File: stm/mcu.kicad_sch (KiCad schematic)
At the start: 46 parts, among them J1 Conn_02x07_Odd_Even, J2 SD_Card_Receptacle, SW2 SW_Push, U1 REF4132B25DBVR, U2 STM32H730ZBTx, Y3 Crystal_GND24, Y4 Crystal

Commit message: labels
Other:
- note added: "Resonator with integrated capacitors Datasheet, 6.3.10, figure 24"

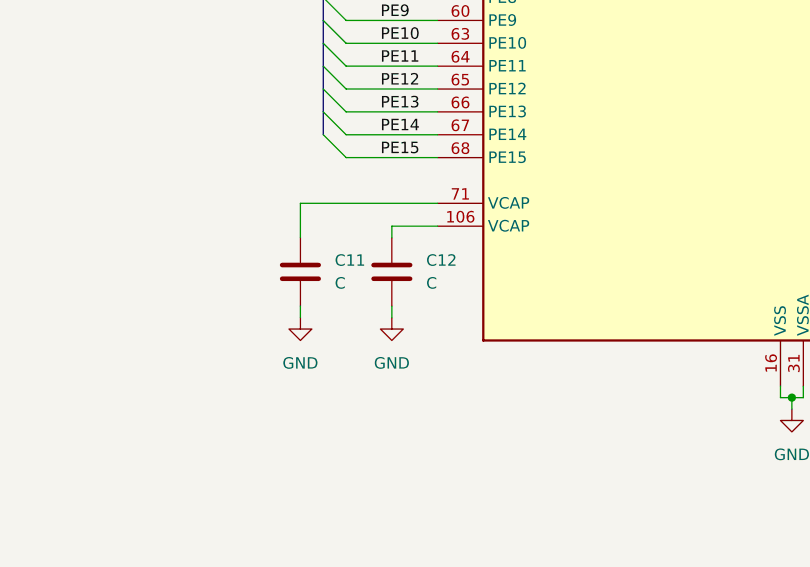
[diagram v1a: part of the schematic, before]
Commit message: vcap on mcu
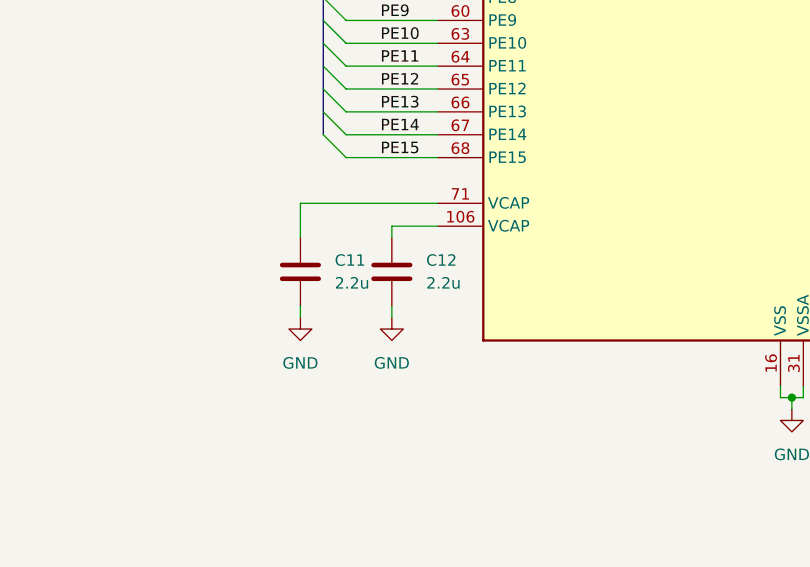
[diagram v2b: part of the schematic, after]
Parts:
- C11, C12: value C -> 2.2u

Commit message: added caps
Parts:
- C1, C10, C15, C16, C17, C18, C19, C21, C22, C23, C24, C25, C26, C3, C7: value C -> 100n
- C13, C14: value C -> 15p
- C2, C20, C4: value C -> 1u
- C27: value C -> 4u7
- C8, C9: value C -> 6p
- R2: value R -> 200k
- Y3: value Crystal_GND24 -> 25MHz
- Y4: value Crystal -> ABS05-32.768KHZ-T

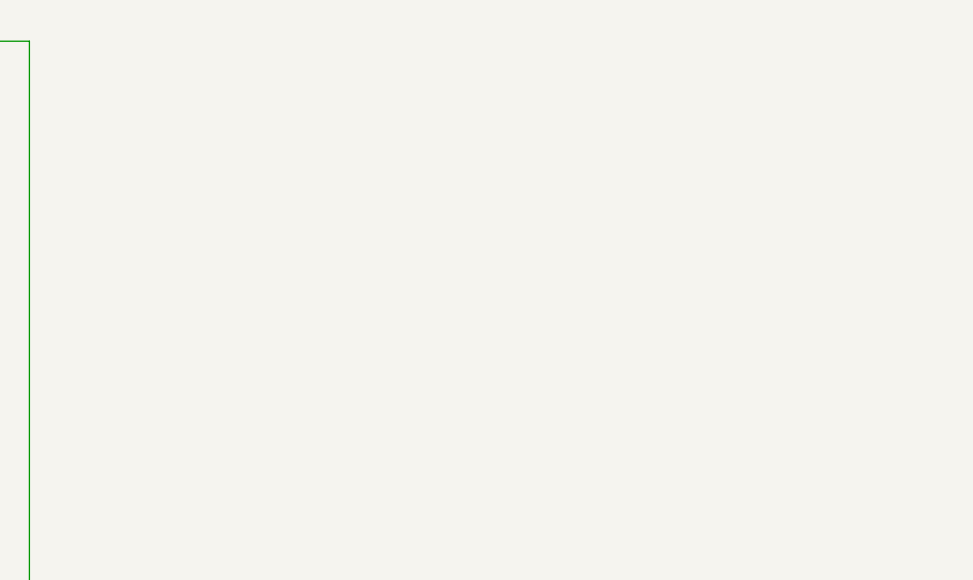
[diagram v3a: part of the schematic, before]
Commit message: RS-422 transceiver module
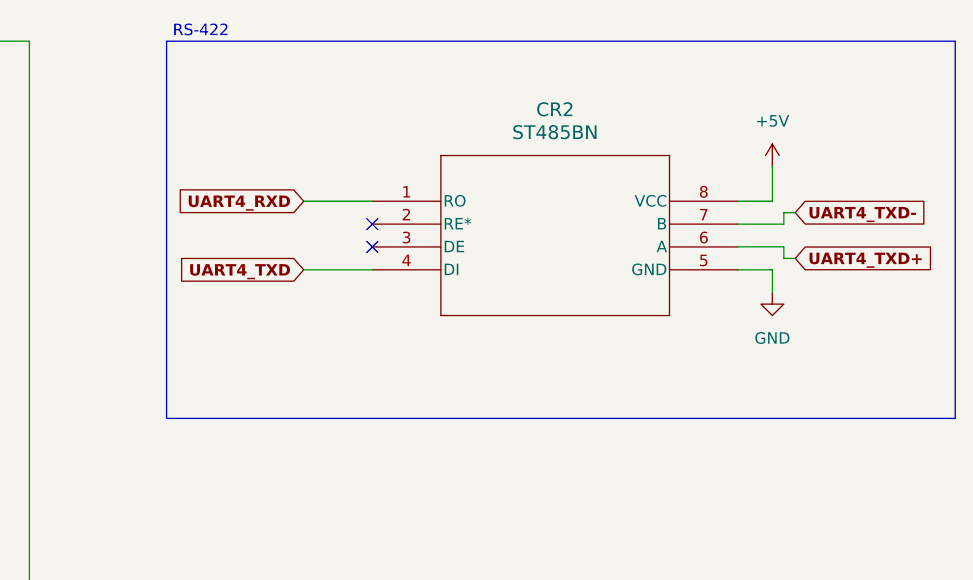
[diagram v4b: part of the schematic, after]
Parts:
- added CR2: ST485BN, SO-8_STM, symbol 2025-09-02_01-37-02:ST485BN
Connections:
- net GND: now also CR2.5 (GND)
- net UART4_RXD: now also CR2.1 (RO)
- net UART4_TXD: now also CR2.4 (DI)
- new net +5V: CR2.8 (VCC)
- new net UART4_TXD+: CR2.6 (A)
- new net UART4_TXD-: CR2.7 (B)
- no-connect marks 4 -> 6
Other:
- note added: "RS-422"

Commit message: Added RS-422 transceiver footprint
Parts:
- CR1: footprint UDFN18_517BV_ONS -> (none)
- CR2: footprint SO-8_STM -> ST485BN:SO-8_STM
- U1: footprint SOT-23-5_DBV_TEX -> (none)

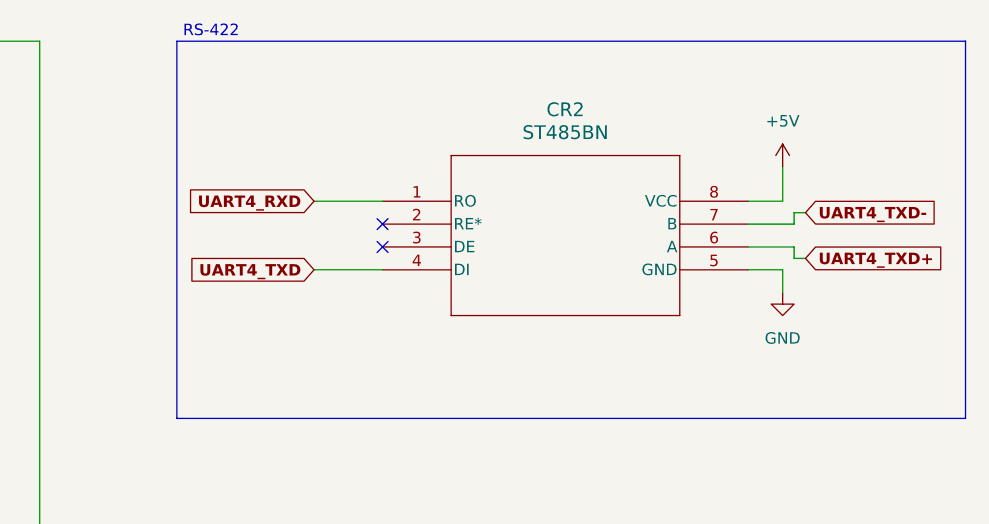
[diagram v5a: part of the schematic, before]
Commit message: Changed part schematic and footprint to ST485BDR
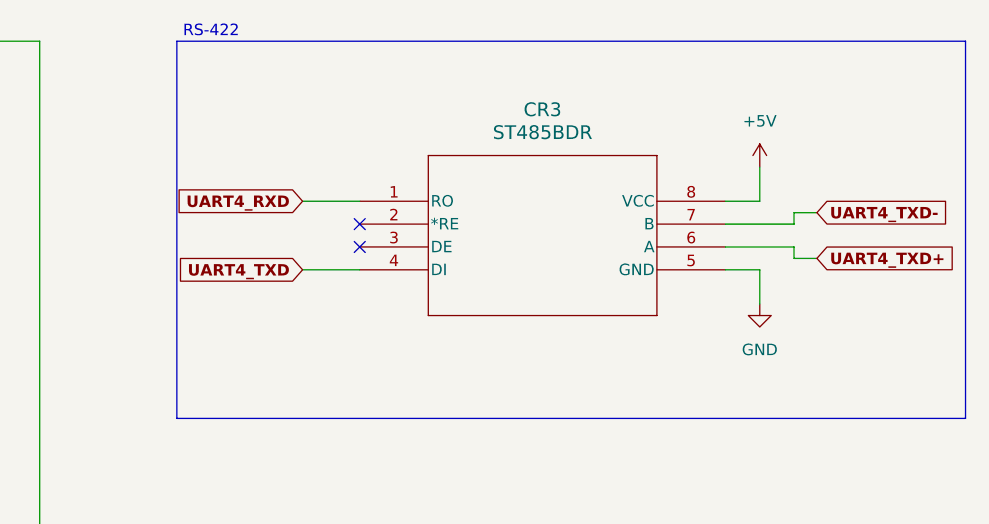
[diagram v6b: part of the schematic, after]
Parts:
- removed CR2: ST485BN, ST485BN:SO-8_STM, symbol 2025-09-02_01-37-02:ST485BN
- added CR3: ST485BDR, ST485BDR:SO-8_STM, symbol 2025-09-03_13-52-52:ST485BDR
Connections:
- net +5V: now also CR3.8 (VCC)
- net GND: now also CR3.5 (GND)
- net UART4_RXD: now also CR3.1 (RO)
- net UART4_TXD: now also CR3.4 (DI)
- net UART4_TXD+: now also CR3.6 (A)
- net UART4_TXD-: now also CR3.7 (B)

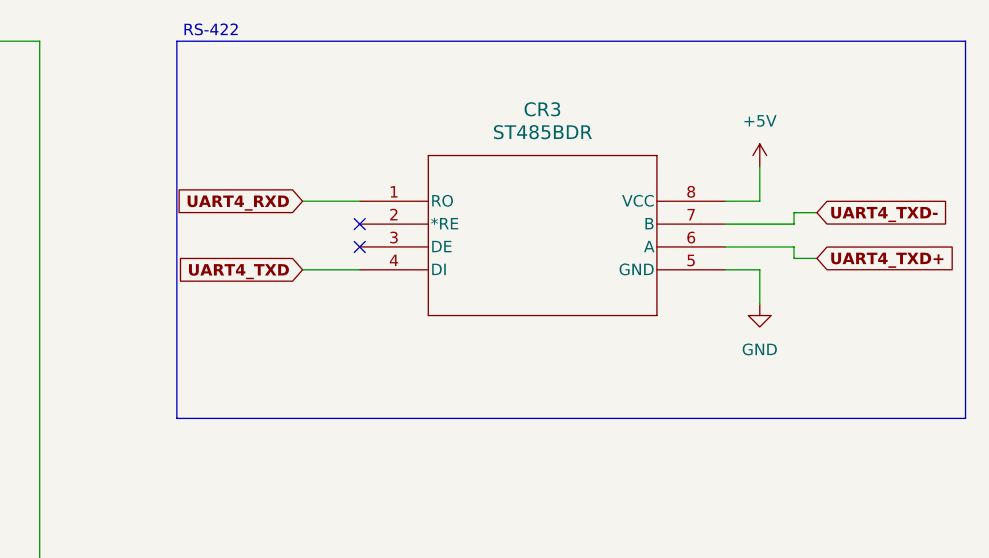
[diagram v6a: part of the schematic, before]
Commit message: added footprint and symbol library
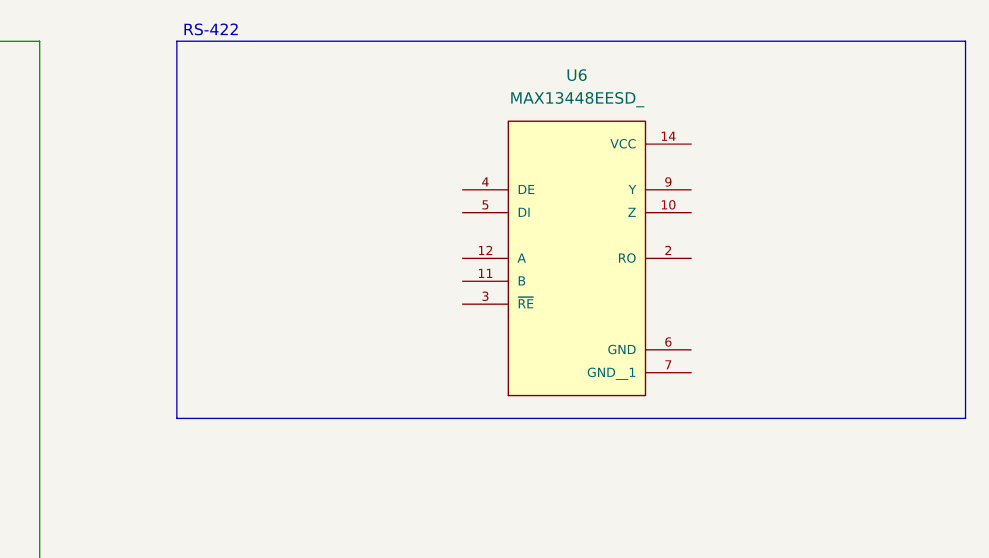
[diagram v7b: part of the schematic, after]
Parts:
- removed CR3: ST485BDR, ST485BDR:SO-8_STM, symbol 2025-09-03_13-52-52:ST485BDR
- added U6: MAX13448EESD_, MAX13448EESD_:SOIC127P600X175-14N, symbol MAX13448EESD:MAX13448EESD_
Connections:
- no-connect marks 6 -> 4

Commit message: added MAX footprint
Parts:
- U6: footprint MAX13448EESD_:SOIC127P600X175-14N -> MAX13448EESD:SOIC127P600X175-14N
